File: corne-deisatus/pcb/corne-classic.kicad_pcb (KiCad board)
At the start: 2 copper layers, 133.8 x 92.2 mm, 98 parts, among them J1 MJ-4PP-9, J2 OLED, J3 LED, P1 i2c-pin, P2 i2c-pin, SW1 SW_PUSH, SW10 SW_PUSH, SW11 SW_PUSH, SW12 SW_PUSH, SW13 SW_PUSH, SW14 SW_PUSH, SW15 SW_PUSH, SW16 SW_PUSH, SW17 SW_PUSH, SW18 SW_PUSH, SW19 SW_PUSH, SW2 SW_PUSH, SW20 SW_PUSH, SW21 SW_PUSH, SW3 SW_PUSH, SW4 SW_PUSH, SW5 SW_PUSH, SW6 SW_PUSH, SW7 SW_PUSH, SW8 SW_PUSH, SW9 SW_PUSH, U1 ProMicro

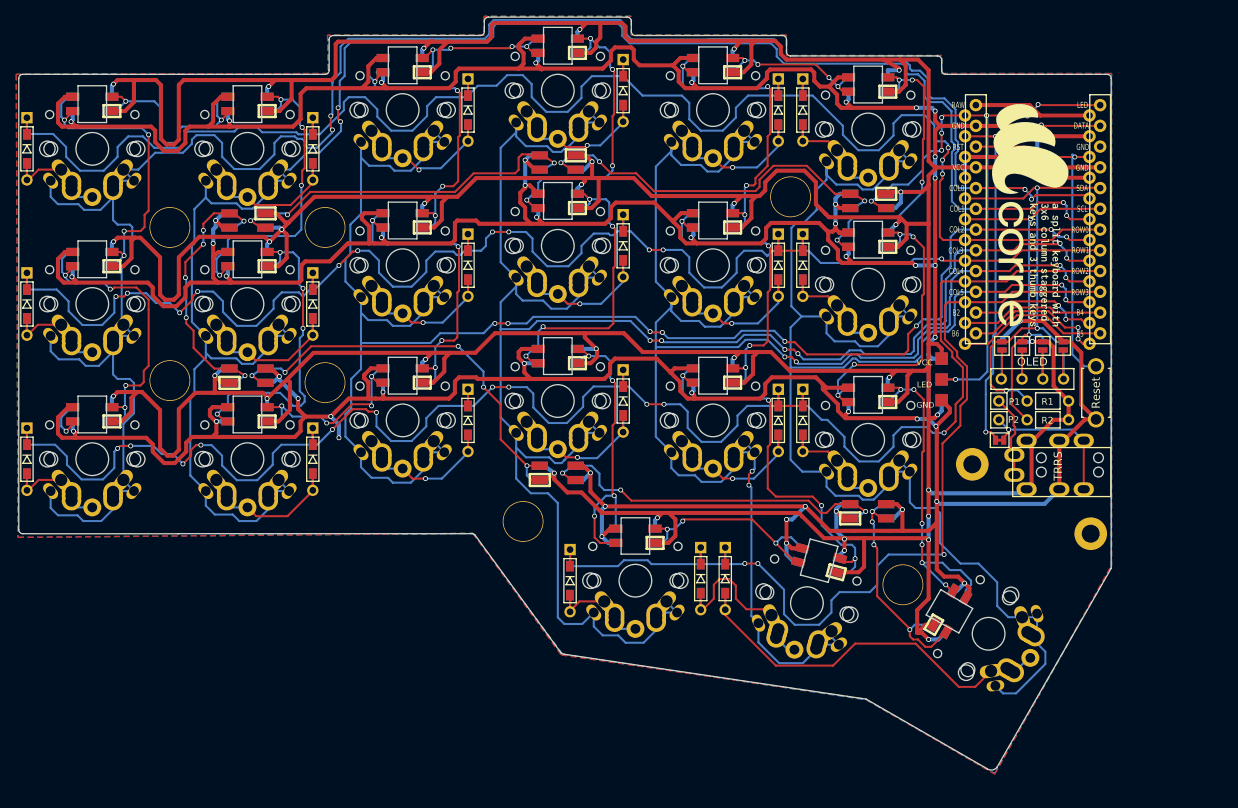
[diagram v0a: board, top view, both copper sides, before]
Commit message: added new footprints and outline
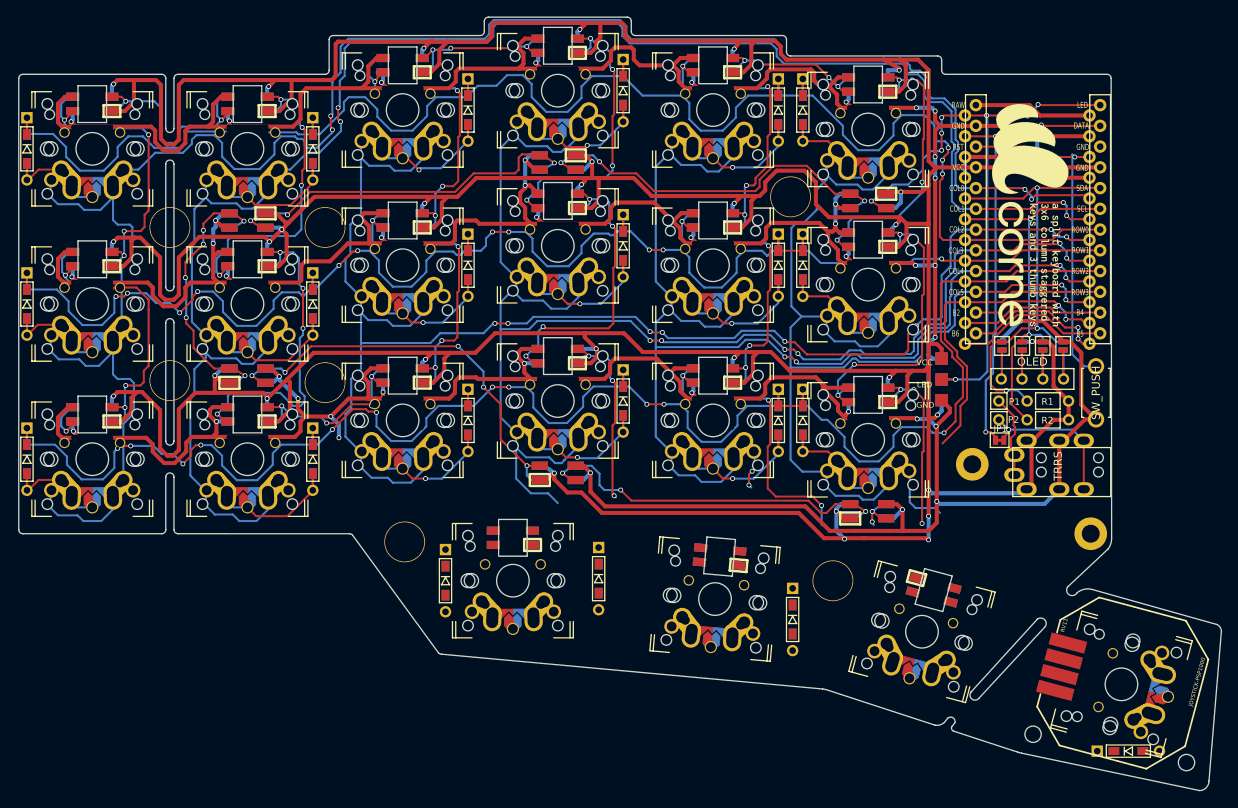
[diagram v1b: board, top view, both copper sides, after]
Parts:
- added D22: D, kbd:D3_TH_SMD, F.Cu at (196.9, 150.9)
- added RV11: JOYSTICK-PSP1000, HackPack_Footprints:JOYSTICK-PSP1000, F.Cu at (196.2, 142.5)
- added SW19: SW_PUSH, kailh-pg1425-x-switch:MX-ALPS-Choc-X-straight-crane, F.Cu at (196.0, 142.7)
- JP1: footprint kbd:JPC2 -> kbd:JP
- RSW1: value Reset -> SW_PUSH
- SW1, SW10, SW11, SW12, SW13, SW14, SW15, SW16, SW17, SW18, SW2, SW3, SW4, SW5, SW6, SW7, SW8, SW9: footprint kbd:MX_ALPS_PG1350_noLed -> kailh-pg1425-x-switch:MX-ALPS-Choc-X-straight-crane
- SW20: renamed from SW19; footprint kbd:MX_ALPS_PG1350_noLed -> kailh-pg1425-x-switch:MX-ALPS-Choc-X-straight-crane
- SW21: renamed from SW20; footprint kbd:MX_ALPS_PG1350_noLed -> kailh-pg1425-x-switch:MX-ALPS-Choc-X-straight-crane-u1.5
- SW22: renamed from SW21; footprint kbd:MX_ALPS_PG1350_noLed_1.75u -> kailh-pg1425-x-switch:MX-ALPS-Choc-X-straight-crane-u1.5
- moved D19 15.2 mm to (113.2, 130.0)
- moved L25 15.0 mm to (121.5, 124.8)
- moved SW20 15.0 mm to (121.5, 130.0)
- moved ? 14.7 mm to (108.2, 125.2)
- moved D20 12.5 mm to (132.0, 129.8)
- moved L26 12.2 mm to (146.8, 127.0), turned to 355 degrees
- moved SW21 11.3 mm to (146.2, 132.2), turned to 175 degrees
- moved D21 9.65 mm to (155.8, 134.8)
- moved ? 8.58 mm to (160.7, 130.0)
- moved SW22 8.16 mm to (171.6, 136.2), turned to 165 degrees
- moved L27 3.27 mm to (173.0, 131.2), turned to 165 degrees
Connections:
- U1 pad 13: Net-(U1-Pad13) -> analogY
- U1 pad 14: Net-(U1-Pad14) -> analogX
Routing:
- net row3: track 121.8 -> 39.0 mm, vias 3 -> 0
- net Net-(D21-Pad2): track 49.9 -> 0.00 mm
- net Net-(L15-Pad3): track 38.7 -> 77.2 mm, vias 4 -> 8
- net Net-(L15-Pad1): track 38.5 -> 0.00 mm, vias 4 -> 0
- net Net-(L18-Pad3): track 38.2 -> 0.00 mm, vias 4 -> 0
- net Net-(L13-Pad3): track 37.7 -> 74.8 mm, vias 4 -> 8
- net Net-(L13-Pad1): track 37.1 -> 0.00 mm, vias 4 -> 0
- net VCC: track 758.8 -> 721.8 mm, vias 33 -> 30
- net col3: track 225.1 -> 189.0 mm
- net col5: track 187.0 -> 151.0 mm
- net Net-(L12-Pad1): track 0.00 -> 35.9 mm, vias 0 -> 4
- net GND: track 797.7 -> 764.2 mm, vias 49 -> 43
- net col4: track 194.3 -> 161.0 mm
- net Net-(L25-Pad3): track 27.9 -> 0.00 mm, vias 3 -> 0
- net Net-(L20-Pad3): track 25.3 -> 0.00 mm, vias 4 -> 0
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- removed copper zone on B.Cu, net GND
- removed copper zone on F.Cu, net GND
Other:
- board size 133.8 x 92.2 mm -> 147.2 x 94.7 mm
- rule pad_to_mask_clearance: 0 -> 0.2
